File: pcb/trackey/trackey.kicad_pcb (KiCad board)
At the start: 2 copper layers, 43.2 x 58.4 mm, 21 parts, among them J1 trackball_port, J2 Audio-Jack-4, J3 COL_port, J4 ROW_port, J6 has_trackball, J7 is_left, U1 Arduino_Pro_Micro, U2 Arduino_Pro_Micro, U3 MCP23S17

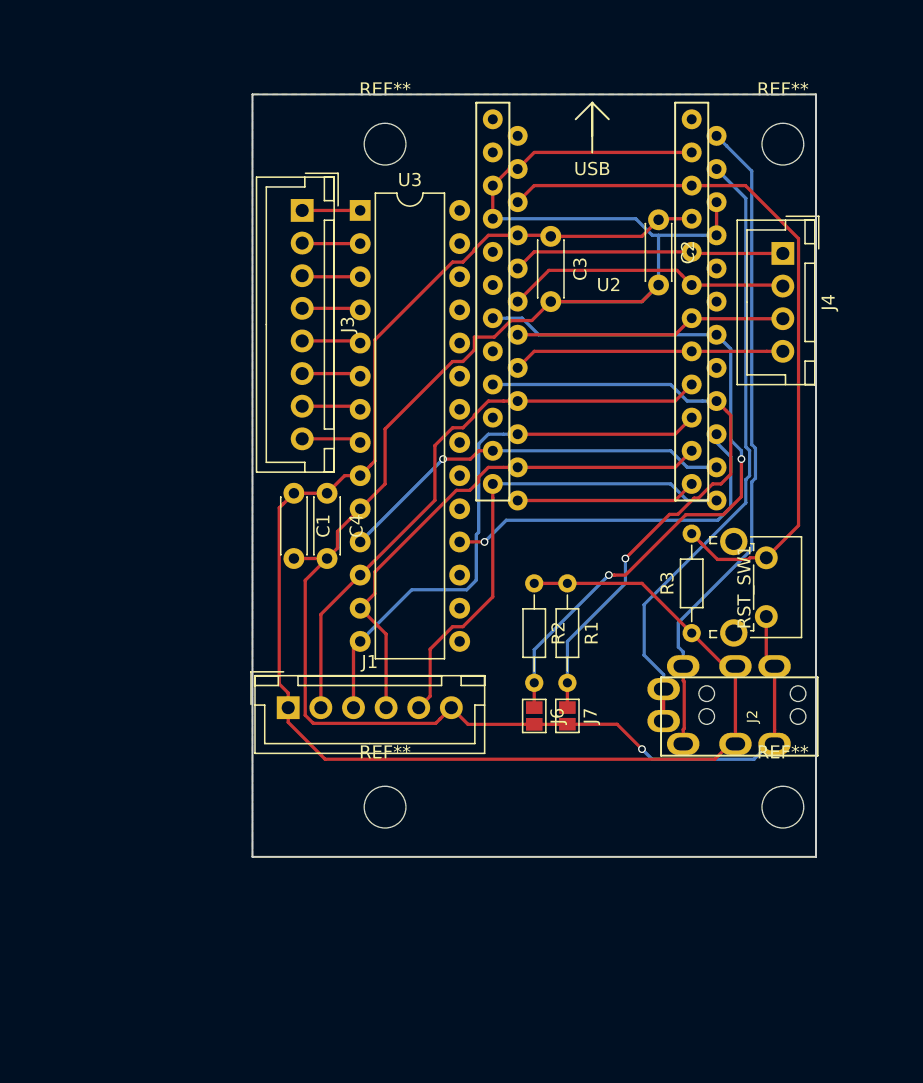
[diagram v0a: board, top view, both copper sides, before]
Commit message: fix main pcb active low
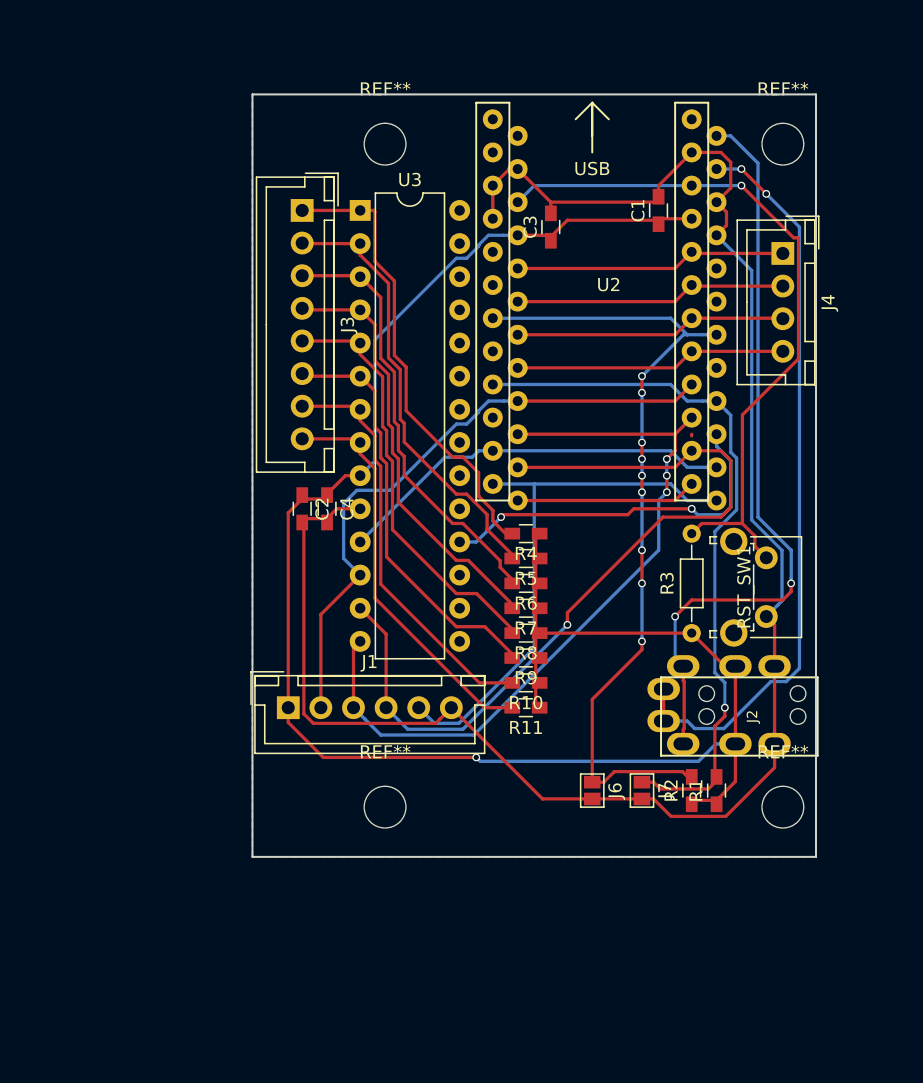
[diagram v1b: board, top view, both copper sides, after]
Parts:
- added R10: 10kΩ, trackey:R_0603, F.Cu at (21.0, 45.1)
- added R11: 10kΩ, trackey:R_0603, F.Cu at (21.0, 47.0)
- added R4: 10kΩ, trackey:R_0603, F.Cu at (21.0, 33.7)
- added R5: 10kΩ, trackey:R_0603, F.Cu at (21.0, 35.6)
- added R6: 10kΩ, trackey:R_0603, F.Cu at (21.0, 37.5)
- added R7: 10kΩ, trackey:R_0603, F.Cu at (21.0, 39.4)
- added R8: 10kΩ, trackey:R_0603, F.Cu at (21.0, 41.3)
- added R9: 10kΩ, trackey:R_0603, F.Cu at (21.0, 43.2)
- C1, C2, C3, C4: footprint Capacitors_THT:C_Disc_D4.3mm_W1.9mm_P5.00mm -> trackey:R_0603
- R1, R2: footprint Resistors_THT:R_Axial_DIN0204_L3.6mm_D1.6mm_P7.62mm_Horizontal -> trackey:R_0603
- moved C1 35.4 mm to (31.1, 8.89), turned to 90 degrees
- moved C2 35.2 mm to (3.81, 31.8)
- moved R2 19.9 mm to (33.7, 53.3), turned to 90 degrees
- moved R1 19.6 mm to (35.6, 53.3), turned to 90 degrees
- moved J7 8.09 mm to (29.8, 53.3)
- moved J6 7.24 mm to (26.0, 53.3)
- moved C4 1.19 mm to (5.71, 31.8)
- moved C3 0.71 mm to (22.9, 10.2), turned to 90 degrees
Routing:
- net /COL0: track 4.45 -> 35.7 mm
- net /COL1: track 4.46 -> 34.0 mm
- net /COL2: track 4.48 -> 33.4 mm
- net /COL3: track 4.49 -> 32.8 mm
- net /COL4: track 4.51 -> 32.6 mm
- net /COL5: track 4.53 -> 32.3 mm
- net /COL6: track 4.54 -> 32.1 mm
- net /COL7: track 4.56 -> 31.3 mm
- net /MOSI: track 40.0 -> 63.9 mm, vias 0 -> 1
- net +5V: track 123.0 -> 140.6 mm, vias 0 -> 1
- net GND: track 153.6 -> 138.0 mm, vias 1 -> 0
- net /MISO: track 43.8 -> 58.7 mm, vias 0 -> 3
- net /RX: track 47.3 -> 57.0 mm, vias 0 -> 2
- net /has_trackball: track 56.0 -> 63.4 mm, vias 2 -> 9
- net /is_left: track 47.7 -> 55.0 mm
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
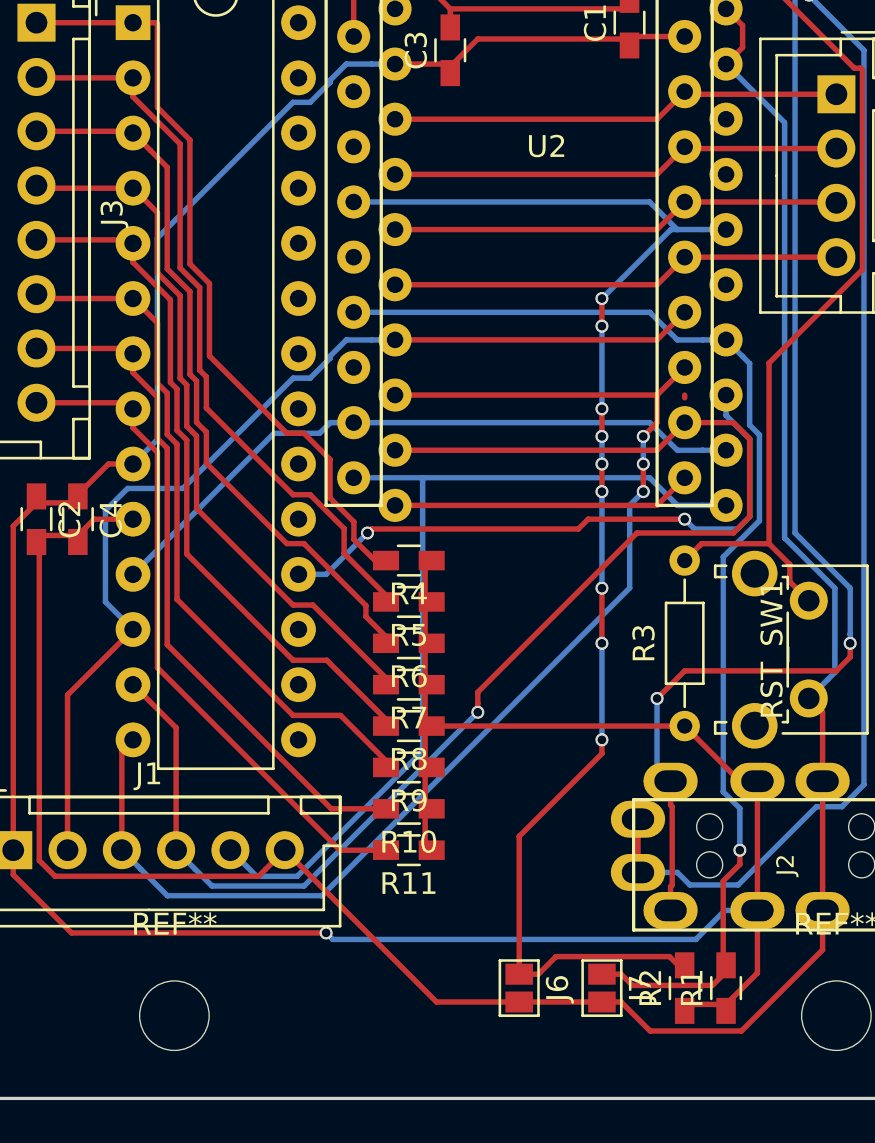
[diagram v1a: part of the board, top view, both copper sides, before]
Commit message: use standard library's footprint
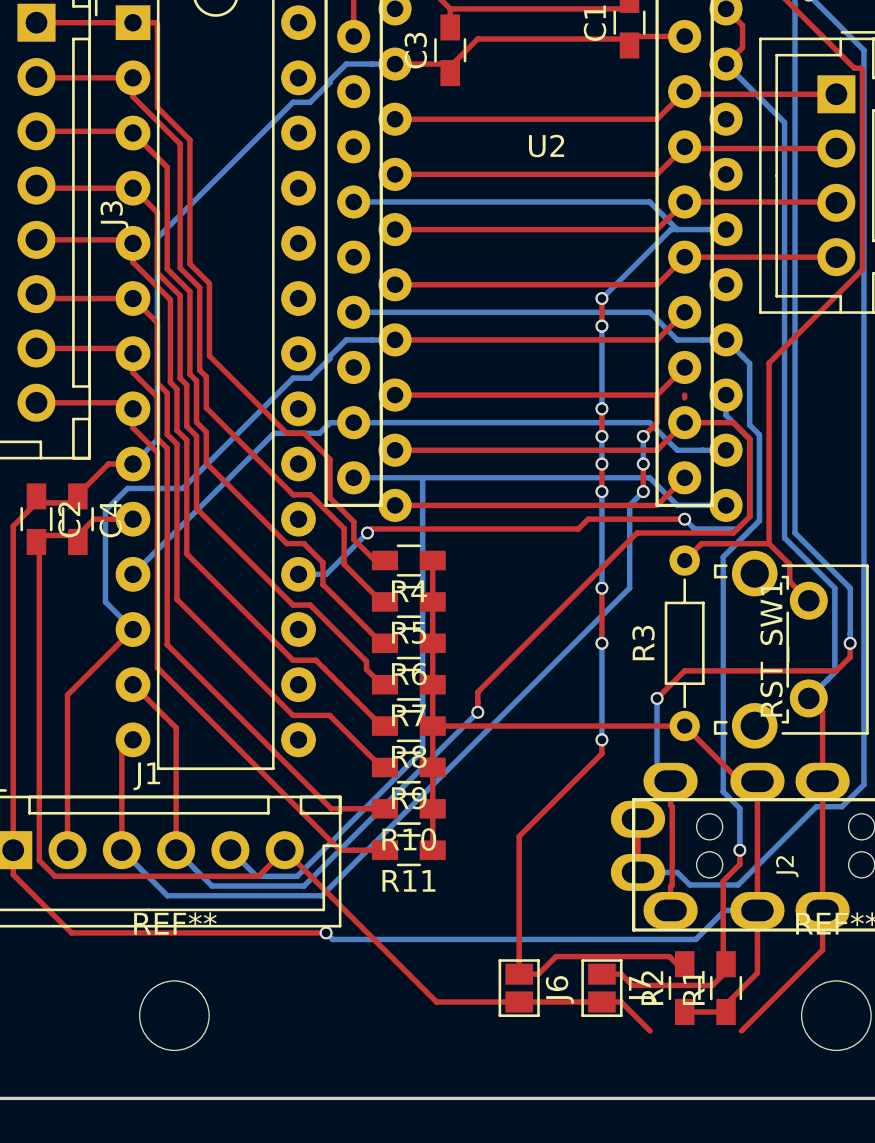
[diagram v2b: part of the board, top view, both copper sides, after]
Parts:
- R1, R10, R11, R2, R4, R5, R6, R7, R8, R9: footprint trackey:R_0603 -> Resistors_SMD:R_0603_HandSoldering
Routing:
- net GND: track 138.0 -> 133.8 mm

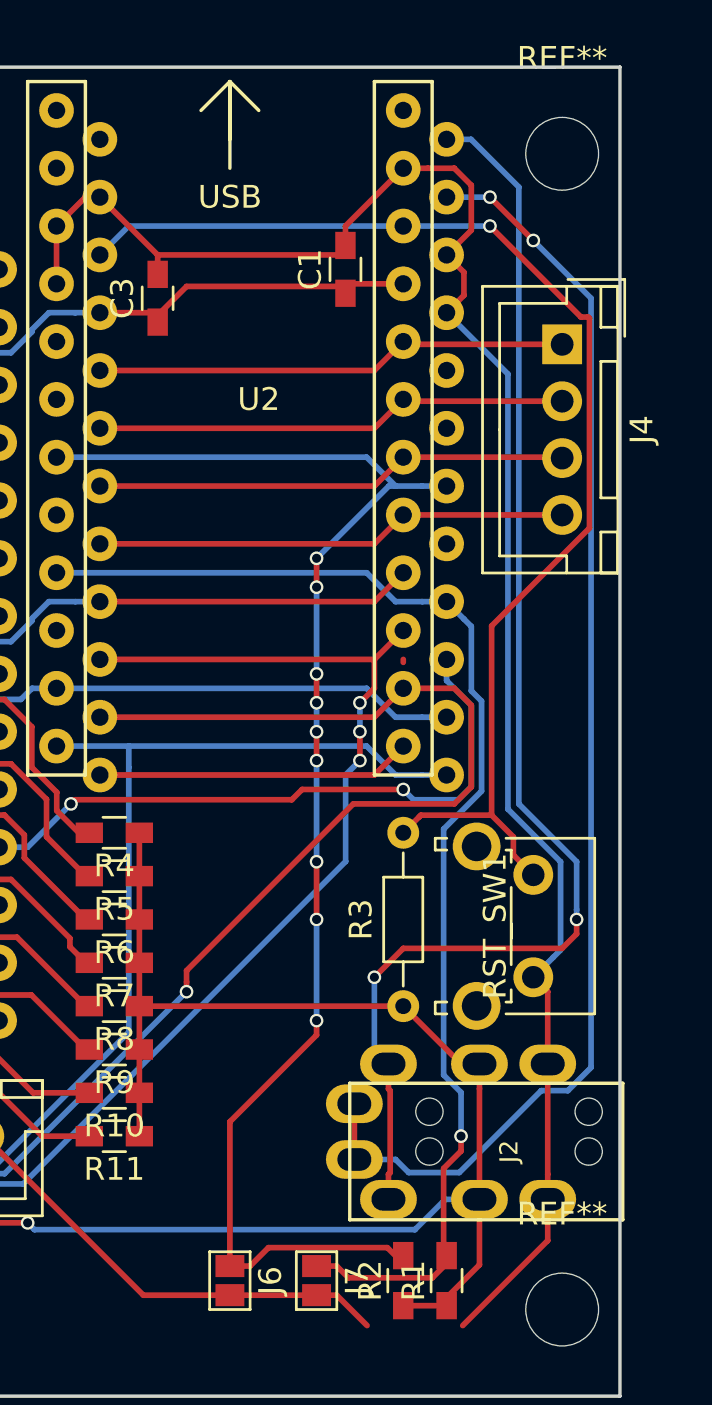
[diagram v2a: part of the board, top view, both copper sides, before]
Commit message: RS-232 -> I2C
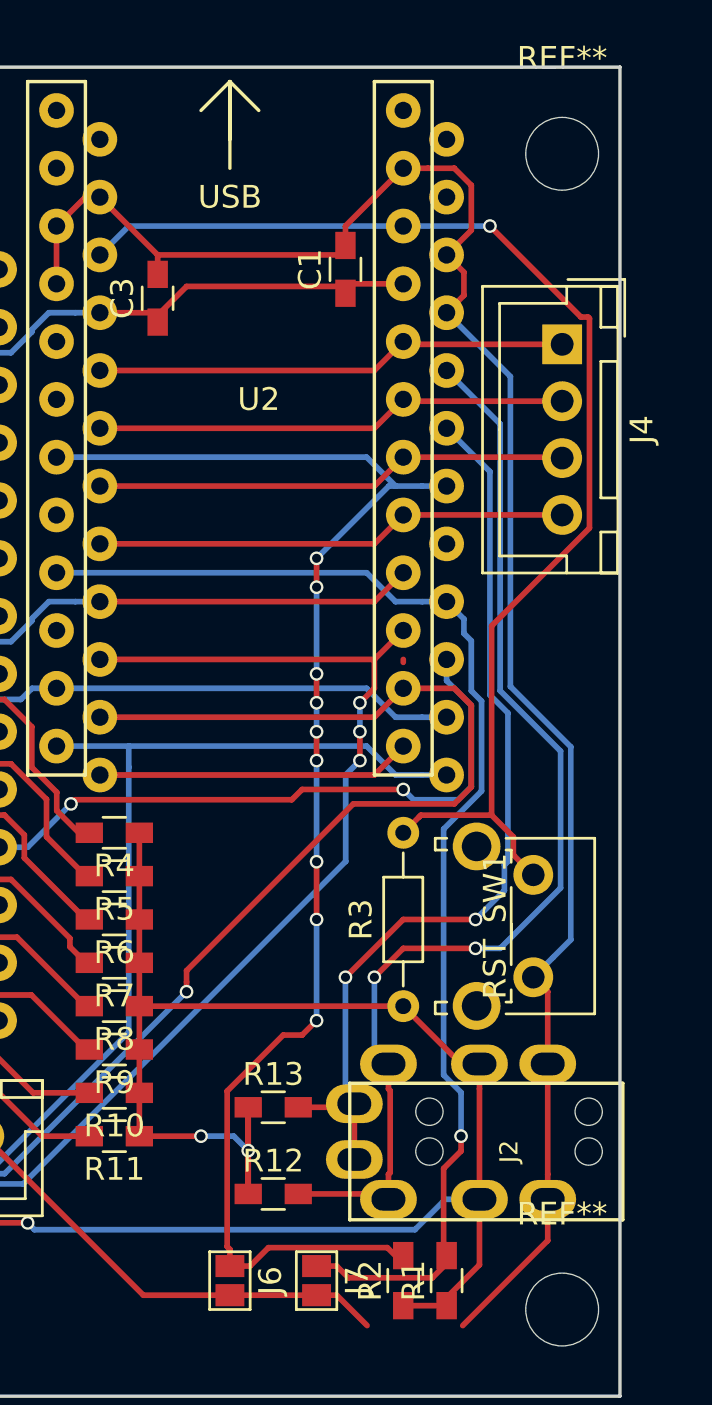
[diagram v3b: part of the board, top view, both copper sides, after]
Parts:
- added R12: 2.2kΩ, Resistors_SMD:R_0603_HandSoldering, F.Cu at (27.9, 49.5)
- added R13: 2.2kΩ, Resistors_SMD:R_0603_HandSoldering, F.Cu at (27.9, 45.7)
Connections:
- J2 pad 1: /RX -> /SCL
- J2 pad 2: /TX -> /SDA
- U1 pad 1: /TX -> Net-(U1-Pad1)
- U1 pad 2: /RX -> Net-(U1-Pad2)
- U1 pad 5: Net-(U1-Pad5) -> /SDA
- U1 pad 6: Net-(U1-Pad6) -> /SCL
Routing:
- net /TX: track 57.7 -> 0.00 mm, vias 2 -> 0
- net /RX: track 57.0 -> 0.00 mm, vias 2 -> 0
- net /SDA: track 0.00 -> 48.8 mm, vias 0 -> 2
- net /SCL: track 0.00 -> 40.8 mm, vias 0 -> 2
- net +5V: track 140.3 -> 153.0 mm, vias 1 -> 3
- net /has_trackball: track 63.4 -> 64.0 mm

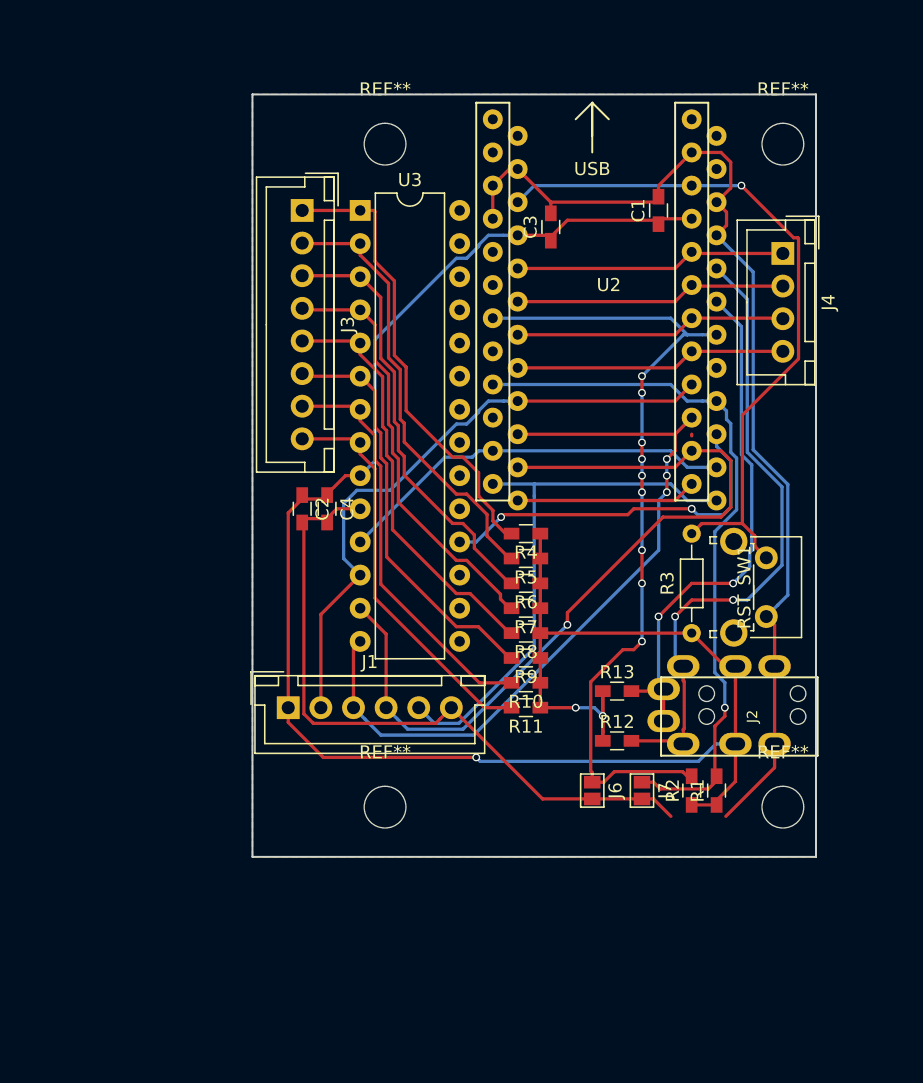
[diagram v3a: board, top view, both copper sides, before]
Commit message: bend XH
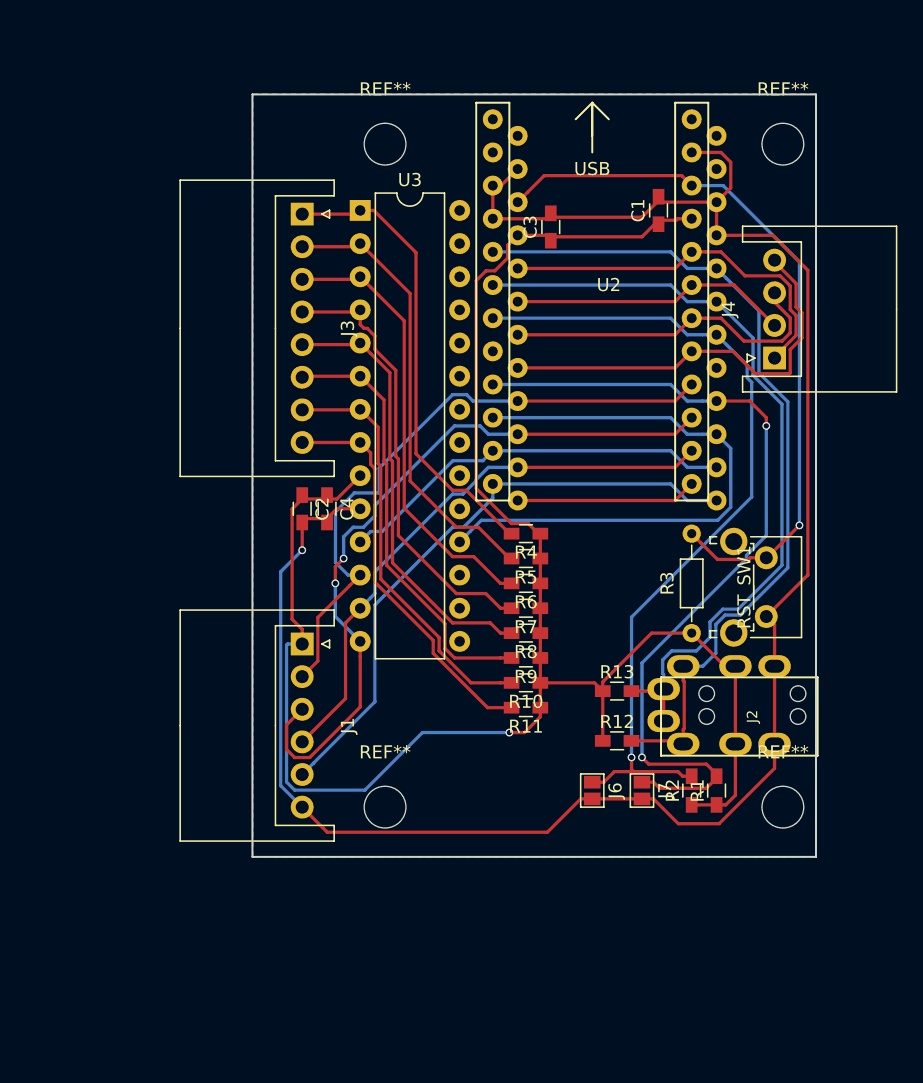
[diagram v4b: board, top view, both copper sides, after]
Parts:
- J1: footprint Connectors_JST:JST_XH_B06B-XH-A_06x2.50mm_Straight -> Connectors_JST:JST_XH_S06B-XH-A_06x2.50mm_Angled
- J3: footprint Connectors_JST:JST_XH_B08B-XH-A_08x2.50mm_Straight -> Connectors_JST:JST_XH_S08B-XH-A_08x2.50mm_Angled
- J4: footprint Connectors_JST:JST_XH_B04B-XH-A_04x2.50mm_Straight -> Connectors_JST:JST_XH_S04B-XH-A_04x2.50mm_Angled
- moved J4 8.04 mm to (40.0, 20.2), turned to 90 degrees
- moved J1 5.00 mm to (3.81, 42.1), turned to 270 degrees
- moved J3 0.28 mm to (3.81, 9.17)
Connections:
- U2 pad 10: Net-(U2-Pad10) -> /Key_IO_RST
- U2 pad 5: Net-(U2-Pad5) -> /SDA
- U2 pad 6: Net-(U2-Pad6) -> /SCL
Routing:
- net /MOSI: track 63.9 -> 43.5 mm, vias 1 -> 0
- net /SCL: track 40.8 -> 60.0 mm, vias 2 -> 0
- net /Key_IO_RST: track 28.3 -> 45.6 mm, vias 2 -> 0
- net /SDA: track 48.8 -> 65.4 mm, vias 2 -> 0
- net GND: track 134.2 -> 148.8 mm, vias 0 -> 1
- net /ROW3: track 20.8 -> 32.0 mm
- net +5V: track 153.0 -> 142.0 mm, vias 3 -> 1
- net /is_left: track 55.0 -> 64.8 mm, vias 1 -> 2
- net /ROW0: track 20.9 -> 28.9 mm
- net /ROW2: track 20.9 -> 26.0 mm
- net /Trackball_SS: track 42.0 -> 46.5 mm
- net /MISO: track 58.7 -> 56.6 mm, vias 3 -> 2
- net /COL4: track 32.2 -> 33.7 mm
- net /COL5: track 32.0 -> 33.4 mm
- net /COL3: track 32.7 -> 34.1 mm
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
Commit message: main pcb:improve circuit layout
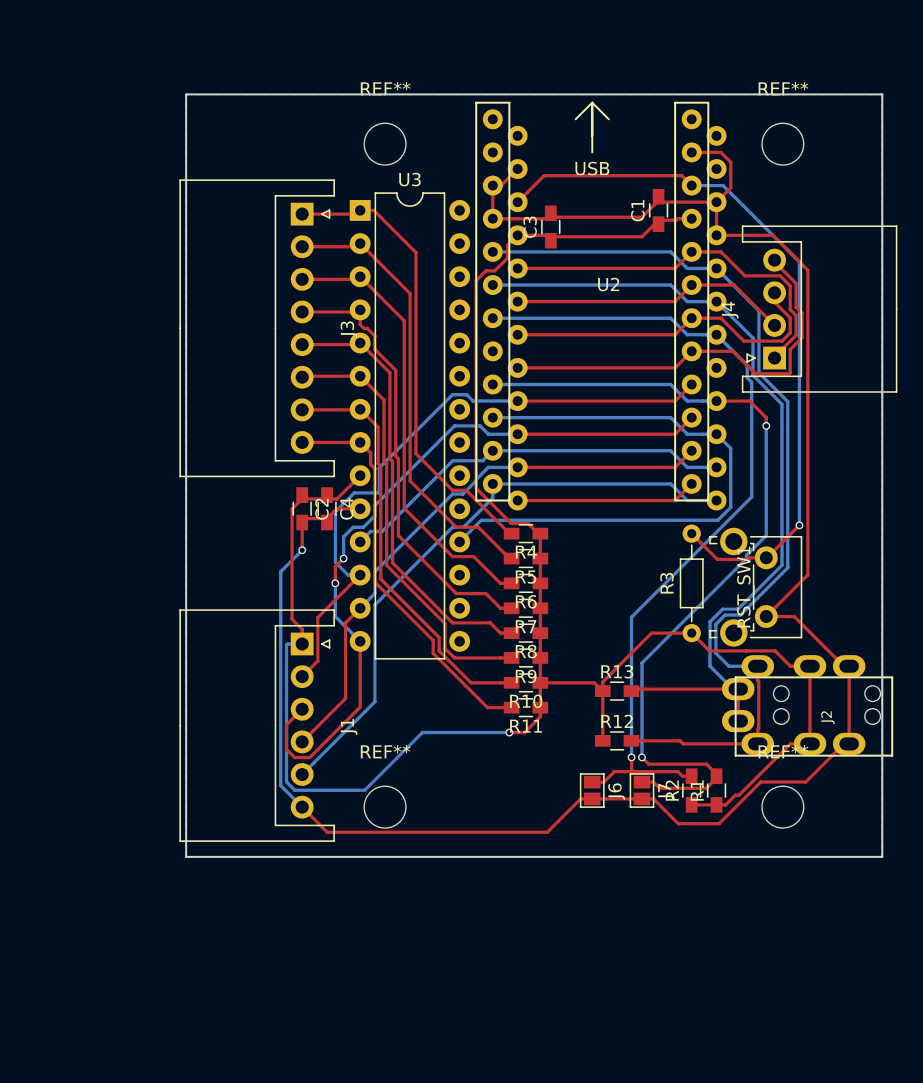
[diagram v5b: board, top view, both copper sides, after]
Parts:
- moved J2 5.72 mm to (49.0, 47.7)
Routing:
- net +5V: track 142.0 -> 151.1 mm
- net GND: track 148.8 -> 157.2 mm
- net /SDA: track 65.4 -> 71.8 mm
- net /SCL: track 60.0 -> 64.2 mm
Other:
- board size 43.2 x 58.4 mm -> 53.3 x 58.4 mm
